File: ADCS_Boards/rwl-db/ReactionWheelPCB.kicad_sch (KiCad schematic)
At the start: 47 parts, among them J1 PC104_Connector, U1 Controller 1, U10 LM358, U2 Controller 3, U3 Conn_1, U4 Conn_3, U5 Controller 2, U6 Controller 4, U7 Conn_2, U8 Conn_4, U9 LM358

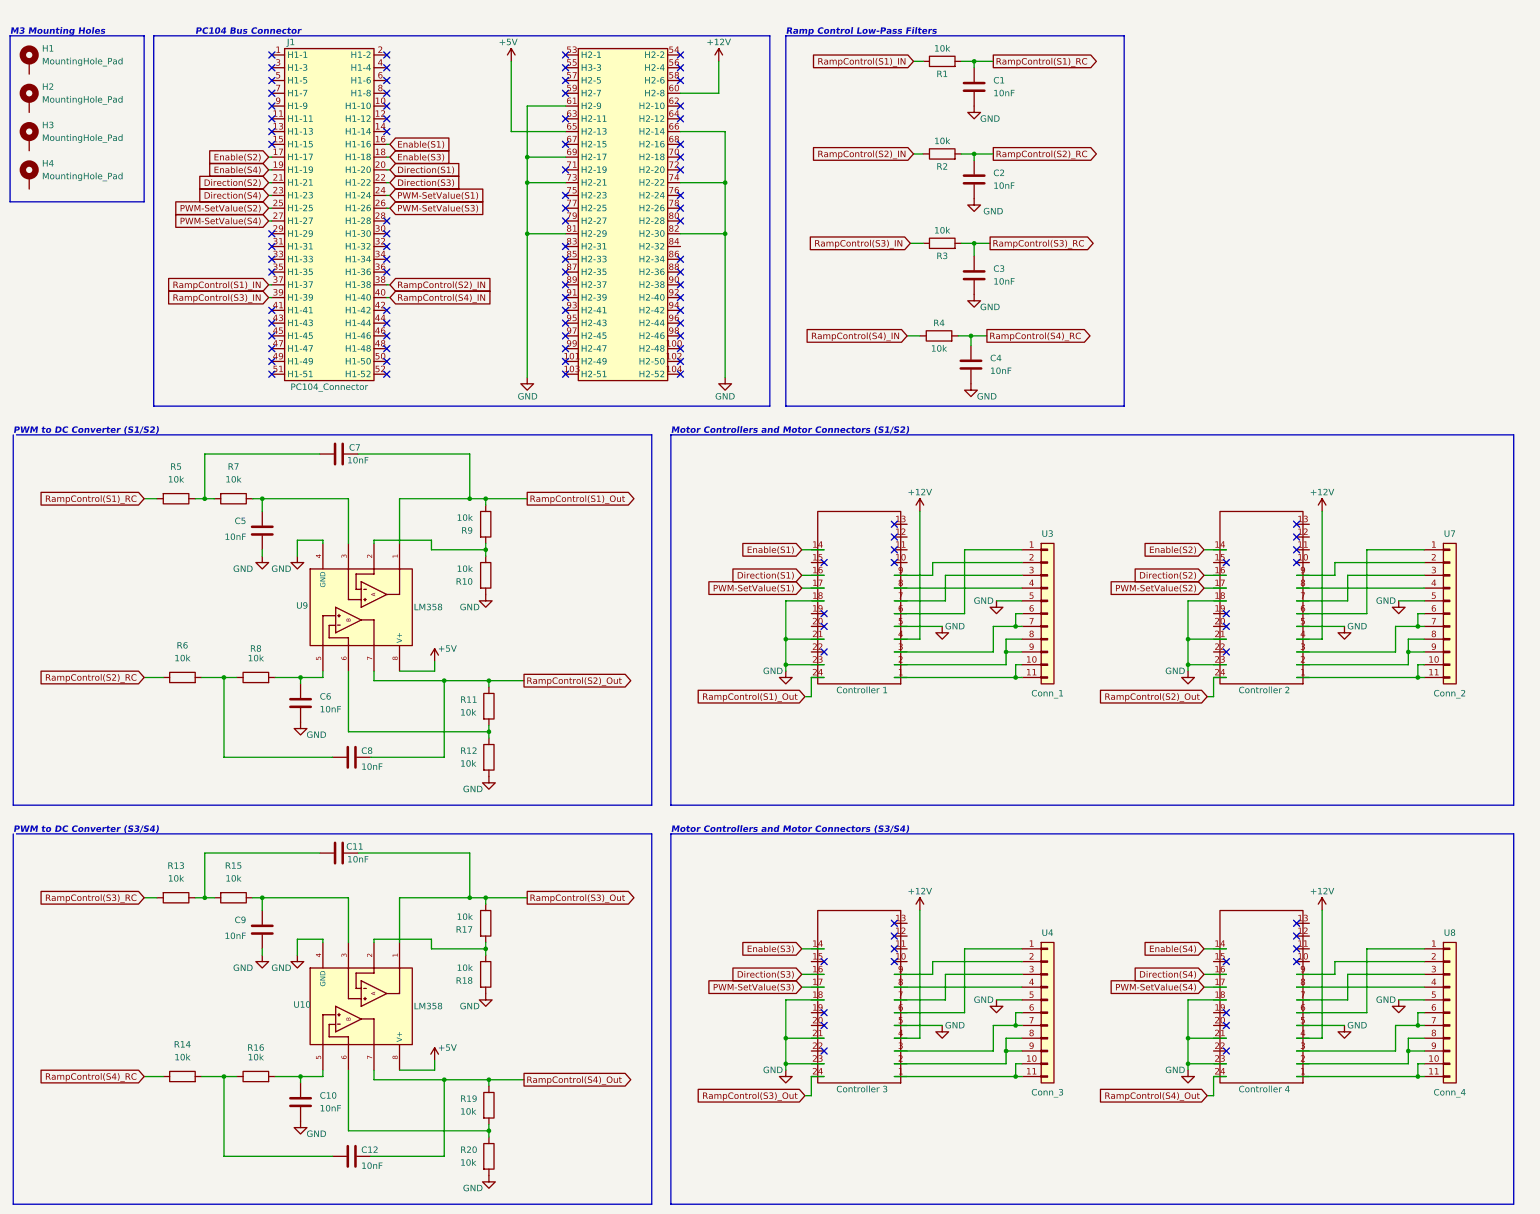
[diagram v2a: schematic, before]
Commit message: adcs: rwl-db: finish layout for controllers 3 and 4
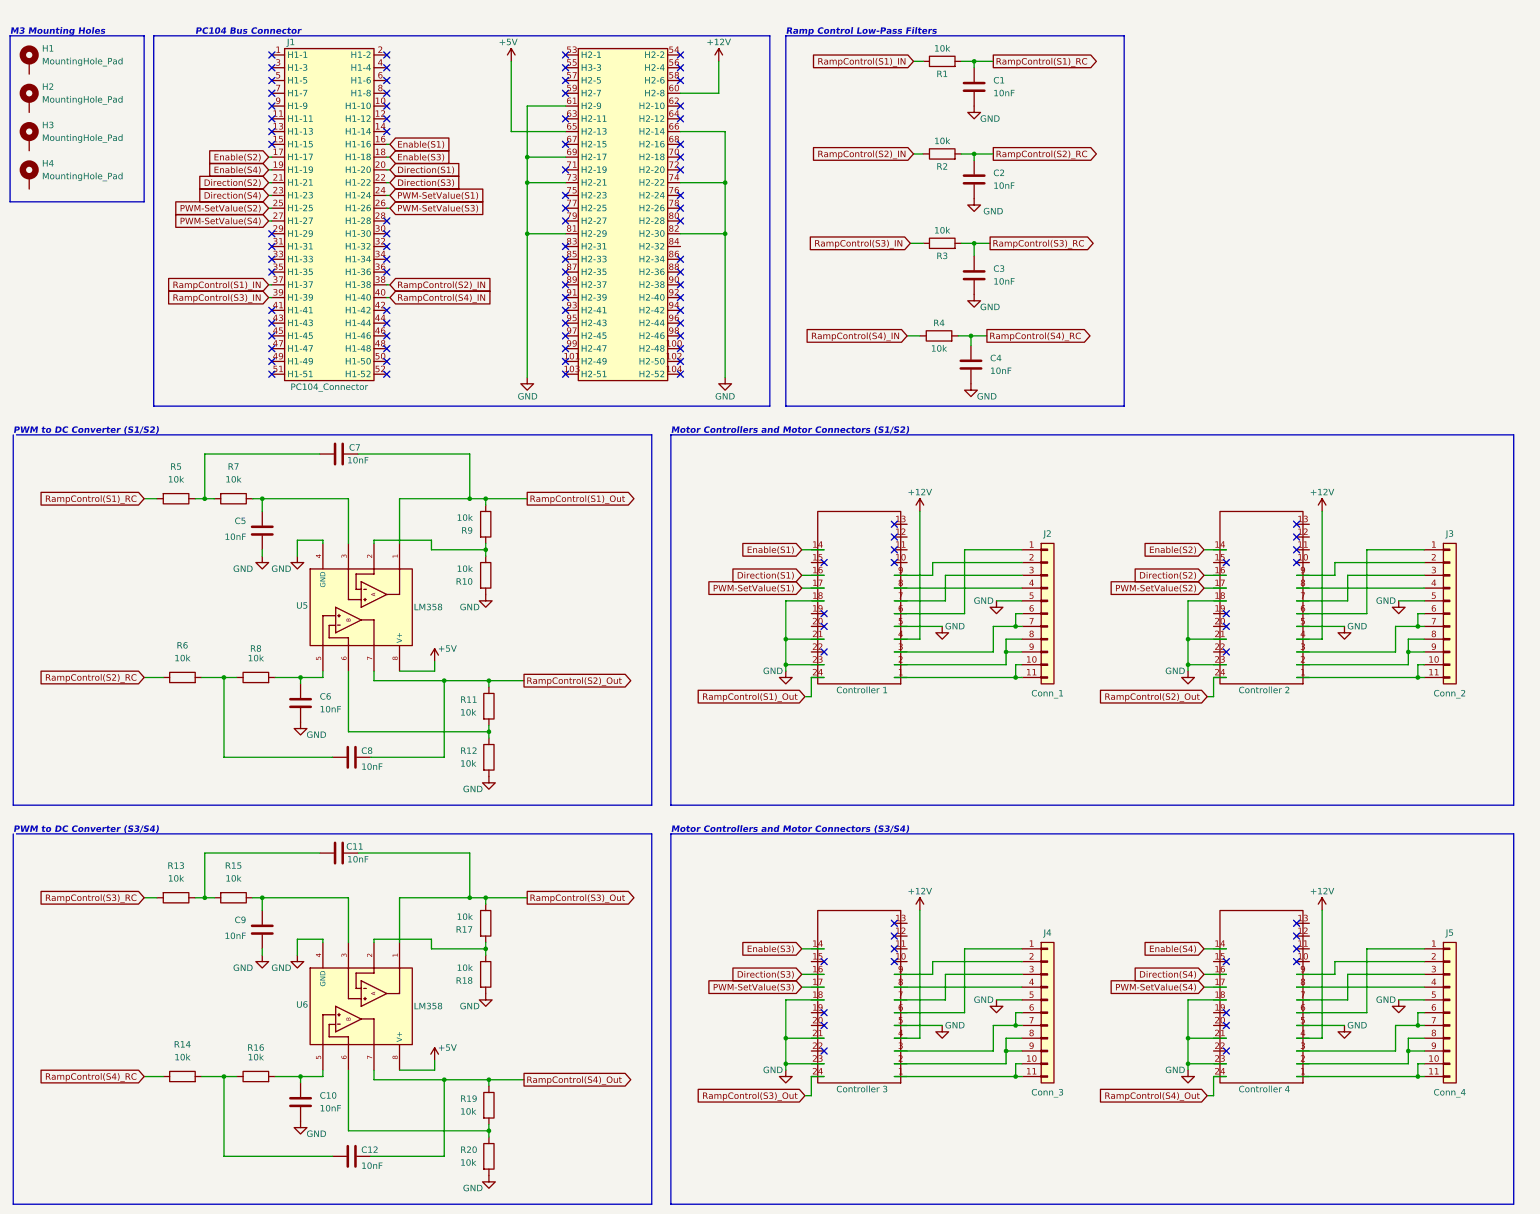
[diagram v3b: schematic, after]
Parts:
- J2: renamed from U3; footprint Footprints_QSAT:FPC_11_SAT_1-84953-1 -> qset-footprints:FPC_11_SAT_1-84953-1
- J3: renamed from U7; footprint Footprints_QSAT:FPC_11_SAT_1-84953-1 -> qset-footprints:FPC_11_SAT_1-84953-1
- J4: renamed from U4; footprint Footprints_QSAT:FPC_11_SAT_1-84953-1 -> qset-footprints:FPC_11_SAT_1-84953-1
- J5: renamed from U8; footprint Footprints_QSAT:FPC_11_SAT_1-84953-1 -> qset-footprints:FPC_11_SAT_1-84953-1
- U1: footprint Footprints_QSAT:Escon24.2 -> qset-footprints:Escon24.2
- U2: renamed from U5; footprint Footprints_QSAT:Escon24.2 -> qset-footprints:Escon24.2
- U3: renamed from U2; footprint Footprints_QSAT:Escon24.2 -> qset-footprints:Escon24.2
- U4: renamed from U6; footprint Footprints_QSAT:Escon24.2 -> qset-footprints:Escon24.2
- U5: renamed from U9; footprint Footprints_QSAT:DIP794W45P254L959H508Q8 -> qset-footprints:DIP794W45P254L959H508Q8
- U6: renamed from U10; footprint Footprints_QSAT:DIP794W45P254L959H508Q8 -> qset-footprints:DIP794W45P254L959H508Q8
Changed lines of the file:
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@@
   (symbol (lib_id "Connector_Generic:Conn_01x11") (at 220.345 209.55 0) (unit 1)
     (in_bom yes) (on_board yes)
-    (property "Reference" "U4" (id 0) (at 220.345 193.675 0))
+    (property "Reference" "J4" (id 0) (at 220.345 193.675 0))
     (property "Value" "Conn_3" (id 1) (at 220.345 225.425 0))
-    (property "Footprint" "Footprints_QSAT:FPC_11_SAT_1-84953-1" (id 2) (at 220.345 209.55 0)
+    (property "Footprint" "qset-footprints:FPC_11_SAT_1-84953-1" (id 2) (at 220.345 209.55 0)
       (effects (font (size 1.27 1.27)) hide)
     )
@@
   (symbol (lib_id "Connector_Generic:Conn_01x11") (at 300.355 209.55 0) (unit 1)
     (in_bom yes) (on_board yes)
-    (property "Reference" "U8" (id 0) (at 300.355 193.675 0))
+    (property "Reference" "J5" (id 0) (at 300.355 193.675 0))
     (property "Value" "Conn_4" (id 1) (at 300.355 225.425 0))
-    (property "Footprint" "Footprints_QSAT:FPC_11_SAT_1-84953-1" (id 2) (at 300.355 209.55 0)
+    (property "Footprint" "qset-footprints:FPC_11_SAT_1-84953-1" (id 2) (at 300.355 209.55 0)
       (effects (font (size 1.27 1.27)) hide)
     )
@@
   (symbol (lib_id "Connector_Generic:Conn_01x11") (at 300.355 130.175 0) (unit 1)
     (in_bom yes) (on_board yes)
-    (property "Reference" "U7" (id 0) (at 300.355 114.3 0))
+    (property "Reference" "J3" (id 0) (at 300.355 114.3 0))
     (property "Value" "Conn_2" (id 1) (at 300.355 146.05 0))
-    (property "Footprint" "Footprints_QSAT:FPC_11_SAT_1-84953-1" (id 2) (at 300.355 130.175 0)
+    (property "Footprint" "qset-footprints:FPC_11_SAT_1-84953-1" (id 2) (at 300.355 130.175 0)
       (effects (font (size 1.27 1.27)) hide)
     )
@@
   (symbol (lib_id "Connector_Generic:Conn_01x11") (at 220.345 130.175 0) (unit 1)
     (in_bom yes) (on_board yes)
-    (property "Reference" "U3" (id 0) (at 220.345 114.3 0))
+    (property "Reference" "J2" (id 0) (at 220.345 114.3 0))
     (property "Value" "Conn_1" (id 1) (at 220.345 146.05 0))
-    (property "Footprint" "Footprints_QSAT:FPC_11_SAT_1-84953-1" (id 2) (at 220.345 130.175 0)
+    (property "Footprint" "qset-footprints:FPC_11_SAT_1-84953-1" (id 2) (at 220.345 130.175 0)
       (effects (font (size 1.27 1.27)) hide)
     )
@@
   (symbol (lib_id "UpdatedControllerBoardSchematic-rescue:Escon24.2-symbols-Controller_Board-rescue-UpdatedController-rescue") (at 192.405 210.82 270) (unit 1)
     (in_bom yes) (on_board yes)
-    (property "Reference" "U2" (id 0) (at 183.515 207.01 0)
+    (property "Reference" "U3" (id 0) (at 183.515 207.01 0)
       (effects (font (size 1.27 1.27)) hide)
     )
@@
       (effects (font (size 1.27 1.27)) (justify right))
     )
-    (property "Footprint" "Footprints_QSAT:Escon24.2" (id 2) (at 183.515 207.01 0)
+    (property "Footprint" "qset-footprints:Escon24.2" (id 2) (at 183.515 207.01 0)
       (effects (font (size 1.27 1.27)) hide)
     )
@@
   (symbol (lib_id "UpdatedControllerBoardSchematic-rescue:Escon24.2-symbols-Controller_Board-rescue-UpdatedController-rescue") (at 272.415 131.445 270) (unit 1)
     (in_bom yes) (on_board yes)
-    (property "Reference" "U5" (id 0) (at 263.525 127.635 0)
+    (property "Reference" "U2" (id 0) (at 263.525 127.635 0)
       (effects (font (size 1.27 1.27)) hide)
     )
@@
       (effects (font (size 1.27 1.27)) (justify right))
     )
-    (property "Footprint" "Footprints_QSAT:Escon24.2" (id 2) (at 263.525 127.635 0)
+    (property "Footprint" "qset-footprints:Escon24.2" (id 2) (at 263.525 127.635 0)
       (effects (font (size 1.27 1.27)) hide)
     )
@@
   (symbol (lib_id "ADCS_Symbols:LM358") (at 95.25 208.28 270) (unit 1)
     (in_bom yes) (on_board yes)
-    (property "Reference" "U10" (id 0) (at 72.0725 207.9625 90))
+    (property "Reference" "U6" (id 0) (at 72.0725 207.9625 90))
     (property "Value" "LM358" (id 1) (at 97.155 208.28 90))
-    (property "Footprint" "Footprints_QSAT:DIP794W45P254L959H508Q8" (id 2) (at 72.39 208.28 0)
+    (property "Footprint" "qset-footprints:DIP794W45P254L959H508Q8" (id 2) (at 72.39 208.28 0)
       (effects (font (size 1.27 1.27)) hide)
     )
@@
   (symbol (lib_id "UpdatedControllerBoardSchematic-rescue:Escon24.2-symbols-Controller_Board-rescue-UpdatedController-rescue") (at 272.415 210.82 270) (unit 1)
     (in_bom yes) (on_board yes)
-    (property "Reference" "U6" (id 0) (at 263.525 207.01 0)
+    (property "Reference" "U4" (id 0) (at 263.525 207.01 0)
       (effects (font (size 1.27 1.27)) hide)
     )
@@
       (effects (font (size 1.27 1.27)) (justify right))
     )
-    (property "Footprint" "Footprints_QSAT:Escon24.2" (id 2) (at 263.525 207.01 0)
+    (property "Footprint" "qset-footprints:Escon24.2" (id 2) (at 263.525 207.01 0)
       (effects (font (size 1.27 1.27)) hide)
     )
@@
       (effects (font (size 1.27 1.27)) (justify right))
     )
-    (property "Footprint" "Footprints_QSAT:Escon24.2" (id 2) (at 183.515 127.635 0)
+    (property "Footprint" "qset-footprints:Escon24.2" (id 2) (at 183.515 127.635 0)
       (effects (font (size 1.27 1.27)) hide)
     )
@@
   (symbol (lib_id "ADCS_Symbols:LM358") (at 95.25 128.905 270) (unit 1)
     (in_bom yes) (on_board yes)
-    (property "Reference" "U9" (id 0) (at 72.0725 128.5875 90))
+    (property "Reference" "U5" (id 0) (at 72.0725 128.5875 90))
     (property "Value" "LM358" (id 1) (at 97.155 128.905 90))
-    (property "Footprint" "Footprints_QSAT:DIP794W45P254L959H508Q8" (id 2) (at 72.39 128.905 0)
+    (property "Footprint" "qset-footprints:DIP794W45P254L959H508Q8" (id 2) (at 72.39 128.905 0)
       (effects (font (size 1.27 1.27)) hide)
     )
@@
       (reference "J1") (unit 1) (value "PC104_Connector") (footprint "qset-footprints:pc104-connector")
     )
+    (path "/4b089c7c-2798-46eb-995e-68efc8c0ebab"
+      (reference "J2") (unit 1) (value "Conn_1") (footprint "qset-footprints:FPC_11_SAT_1-84953-1")
+    )
+    (path "/2f65813c-da5e-4d09-98bb-345b1c610eb8"
+      (reference "J3") (unit 1) (value "Conn_2") (footprint "qset-footprints:FPC_11_SAT_1-84953-1")
+    )
+    (path "/03844e98-6300-41de-a761-fb59c02fb4c2"
+      (reference "J4") (unit 1) (value "Conn_3") (footprint "qset-footprints:FPC_11_SAT_1-84953-1")
+    )
+    (path "/2cb3ad0d-9460-4819-8e50-5b29b414fe27"
+      (reference "J5") (unit 1) (value "Conn_4") (footprint "qset-footprints:FPC_11_SAT_1-84953-1")
+    )
     (path "/86f52e6c-63f2-4a8b-a27b-32cf82bf3333"
       (reference "R1") (unit 1) (value "10k") (footprint "Resistor_SMD:R_0603_1608Metric")
@@
     )
     (path "/e3ec8df8-257b-4e52-a9f3-16f3fe76a12c"
-      (reference "U1") (unit 1) (value "Controller 1") (footprint "Footprints_QSAT:Escon24.2")
+      (reference "U1") (unit 1) (value "Controller 1") (footprint "qset-footprints:Escon24.2")
+    )
+    (path "/8c768061-02ec-4c2a-b06a-aa69dd275a32"
+      (reference "U2") (unit 1) (value "Controller 2") (footprint "qset-footprints:Escon24.2")
     )
     (path "/62f284b1-998c-46b5-932c-8eeebb75e88c"
-      (reference "U2") (unit 1) (value "Controller 3") (footprint "Footprints_QSAT:Escon24.2")
-    )
-    (path "/4b089c7c-2798-46eb-995e-68efc8c0ebab"
-      (reference "U3") (unit 1) (value "Conn_1") (footprint "Footprints_QSAT:FPC_11_SAT_1-84953-1")
-    )
-    (path "/03844e98-6300-41de-a761-fb59c02fb4c2"
-      (reference "U4") (unit 1) (value "Conn_3") (footprint "Footprints_QSAT:FPC_11_SAT_1-84953-1")
-    )
-    (path "/8c768061-02ec-4c2a-b06a-aa69dd275a32"
-      (reference "U5") (unit 1) (value "Controller 2") (footprint "Footprints_QSAT:Escon24.2")
+      (reference "U3") (unit 1) (value "Controller 3") (footprint "qset-footprints:Escon24.2")
     )
     (path "/b59c5a28-0179-493a-af5e-def20a2ff752"
-      (reference "U6") (unit 1) (value "Controller 4") (footprint "Footprints_QSAT:Escon24.2")
-    )
-    (path "/2f65813c-da5e-4d09-98bb-345b1c610eb8"
-      (reference "U7") (unit 1) (value "Conn_2") (footprint "Footprints_QSAT:FPC_11_SAT_1-84953-1")
-    )
-    (path "/2cb3ad0d-9460-4819-8e50-5b29b414fe27"
-      (reference "U8") (unit 1) (value "Conn_4") (footprint "Footprints_QSAT:FPC_11_SAT_1-84953-1")
+      (reference "U4") (unit 1) (value "Controller 4") (footprint "qset-footprints:Escon24.2")
     )
     (path "/f779d80d-76c7-417d-b22f-8391e145bedd"
-      (reference "U9") (unit 1) (value "LM358") (footprint "Footprints_QSAT:DIP794W45P254L959H508Q8")
+      (reference "U5") (unit 1) (value "LM358") (footprint "qset-footprints:DIP794W45P254L959H508Q8")
     )
     (path "/a91ac937-6db0-4544-a6d5-2fc696e30a86"
-      (reference "U10") (unit 1) (value "LM358") (footprint "Footprints_QSAT:DIP794W45P254L959H508Q8")
-    )
-  )
+      (reference "U6") (unit 1) (value "LM358") (footprint "qset-footprints:DIP794W45P254L959H508Q8")
+    )
+  )
